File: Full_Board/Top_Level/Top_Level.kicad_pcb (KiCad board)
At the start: 2 copper layers, 218 parts, among them IC1 DRV8824QPWPRQ1, IC2 DRV8824QPWPRQ1, IC3 DRV8824QPWPRQ1, IC4 LM2576HVS-5.0_NOPB, IC5 CD74HC4051PWT, IC6 CD74HC4051PWT, IC7 DRV8210DRLR, J1 OQ0212500000G, J1-J1 Conn_01x10, J10 KLDHCX-8-0202-A, J11 OQ0212500000G, J12 OQ0432500000G, J13 OQ0432500000G, J15 OQ0432500000G, J16 OQ0432500000G, J17 OQ0432500000G, J18 OQ0432500000G, J19 OQ0432500000G, J2 OQ0212500000G, J20 OQ0432500000G, J21 OQ0212500000G, J22 OQ0212500000G, J23 OQ0212500000G, J24 OQ0212500000G, J3 OQ0432500000G, J4 OQ0432500000G, J4-J1 Conn_01x10, J5 OQ0432500000G, J5-J1 Conn_01x10, J6 USB_A, J7 OQ0212500000G, J8 OQ0212500000G, J8-J1 Conn_01x10, J9 OQ0212500000G, U1 UCLAMP3301H.TCT, U10 LM2576SX-3.3-NOPB, U11 UCLAMP3301H.TCT, U12 UCLAMP3301H.TCT, U13 UCLAMP3301H.TCT, U14 UCLAMP3301H.TCT, U15 UCLAMP3301H.TCT, U16 UCLAMP3301H.TCT, U17 UCLAMP3301H.TCT, U18 UCLAMP3301H.TCT, U2 UCLAMP3301H.TCT, U3 UCLAMP3301H.TCT, U4 UCLAMP3301H.TCT, U5 UCLAMP3301H.TCT, U6 UCLAMP3301H.TCT, U7 JS102011SCQN, U8 UCLAMP3301H.TCT, U9 UCLAMP3301H.TCT

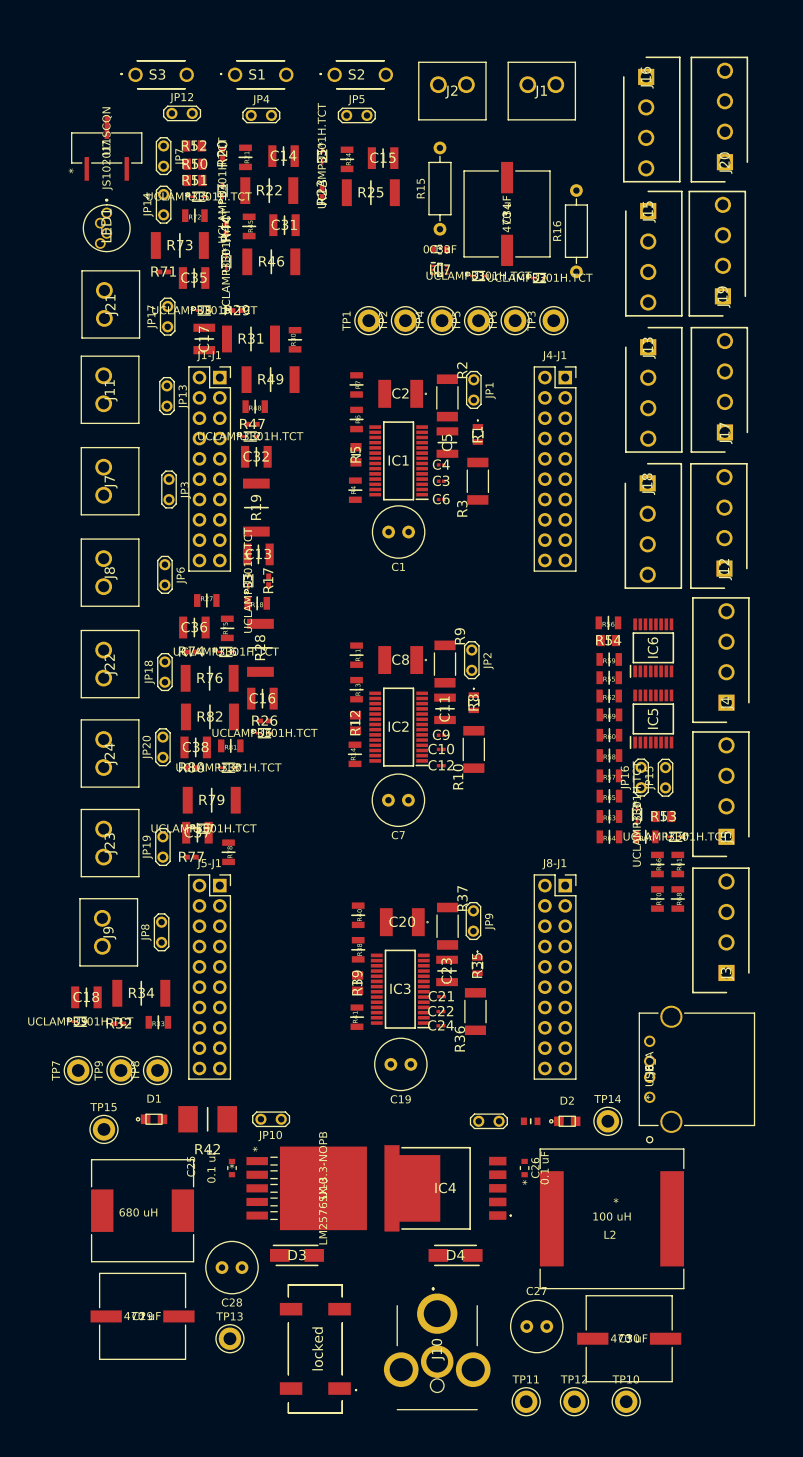
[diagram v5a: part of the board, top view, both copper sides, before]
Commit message: Add GND plane, GND major ICs
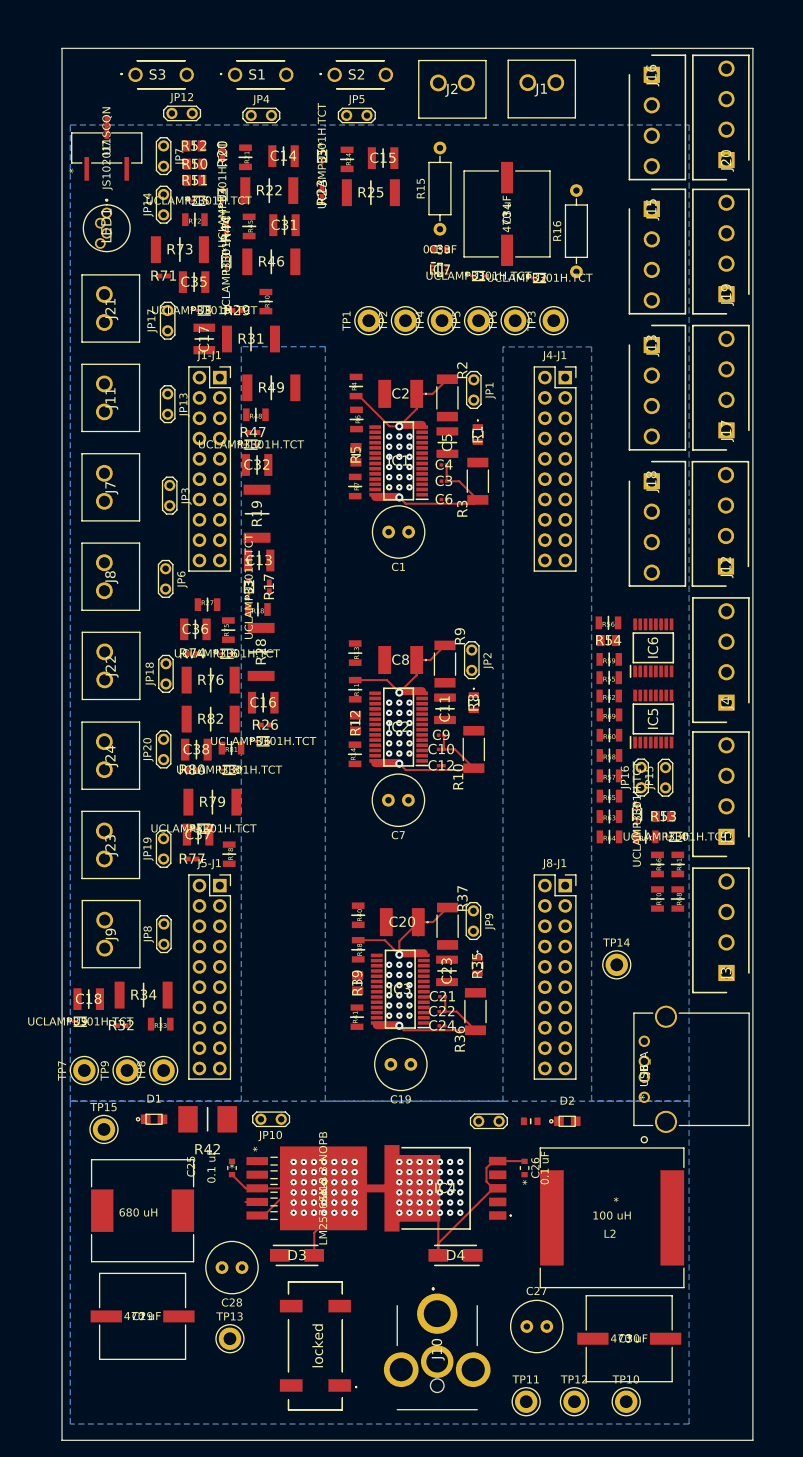
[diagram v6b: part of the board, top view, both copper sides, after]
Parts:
- moved TP14 19.6 mm to (123.8, 133.9)
- moved R4 13.0 mm to (92.0, 60.0)
- moved R7 12.7 mm to (90.3, 75.7)
- moved R30 5.49 mm to (79.1, 52.6), turned to 90 degrees
- moved R13 4.57 mm to (90.3, 96.5)
- moved R11 4.32 mm to (90.3, 101.1)
- moved U6 1.03 mm to (79.6, 105.9)
- moved U12 1.02 mm to (78.1, 68.8)
- moved R47 1.02 mm to (78.3, 67.3)
- moved R48 1.02 mm to (77.1, 64.3)
- moved JP13 1.02 mm to (67.7, 62.5)
- moved J11 1.02 mm to (59.7, 61.2)
- moved R49 1.02 mm to (80.6, 61.7)
- moved C32 1.02 mm to (78.8, 71.4)
- moved R17 0.77 mm to (80.4, 86.6)
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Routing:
- net GND: track 0.00 -> 198.6 mm, vias 0 -> 144
- net Net-(D3-Pad1): track 0.00 -> 2.27 mm
- added copper zone on B.Cu, net GND
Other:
- board outline added: 86.4 x 174 mm

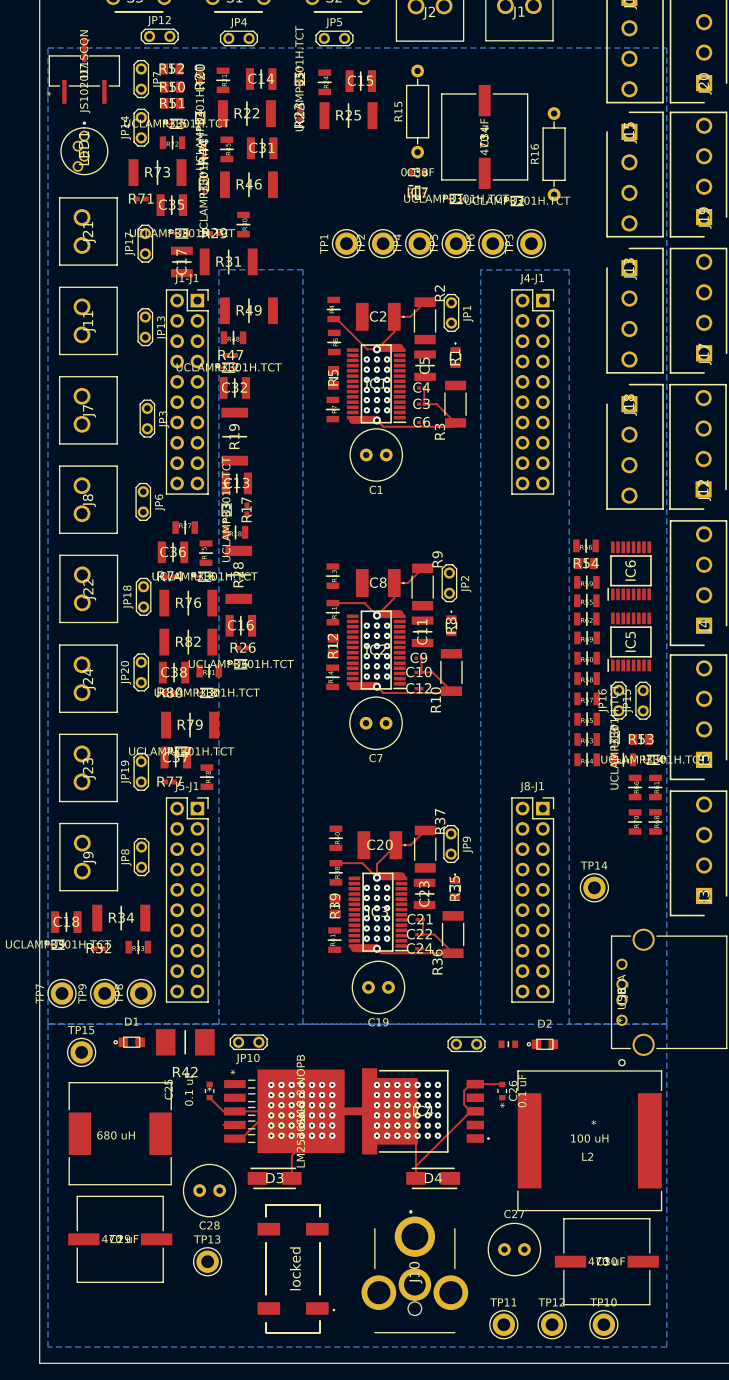
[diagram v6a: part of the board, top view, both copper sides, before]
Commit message: Merge GND planes, update gitignore rules
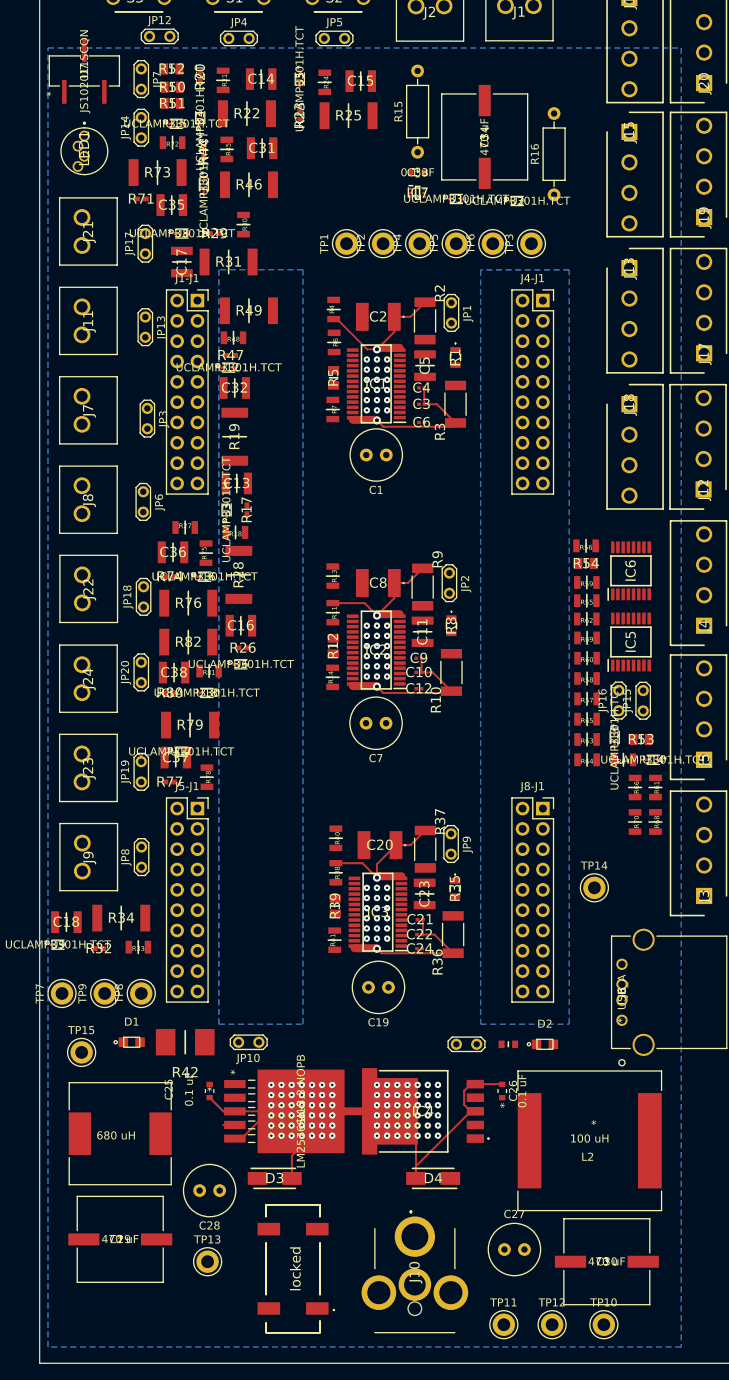
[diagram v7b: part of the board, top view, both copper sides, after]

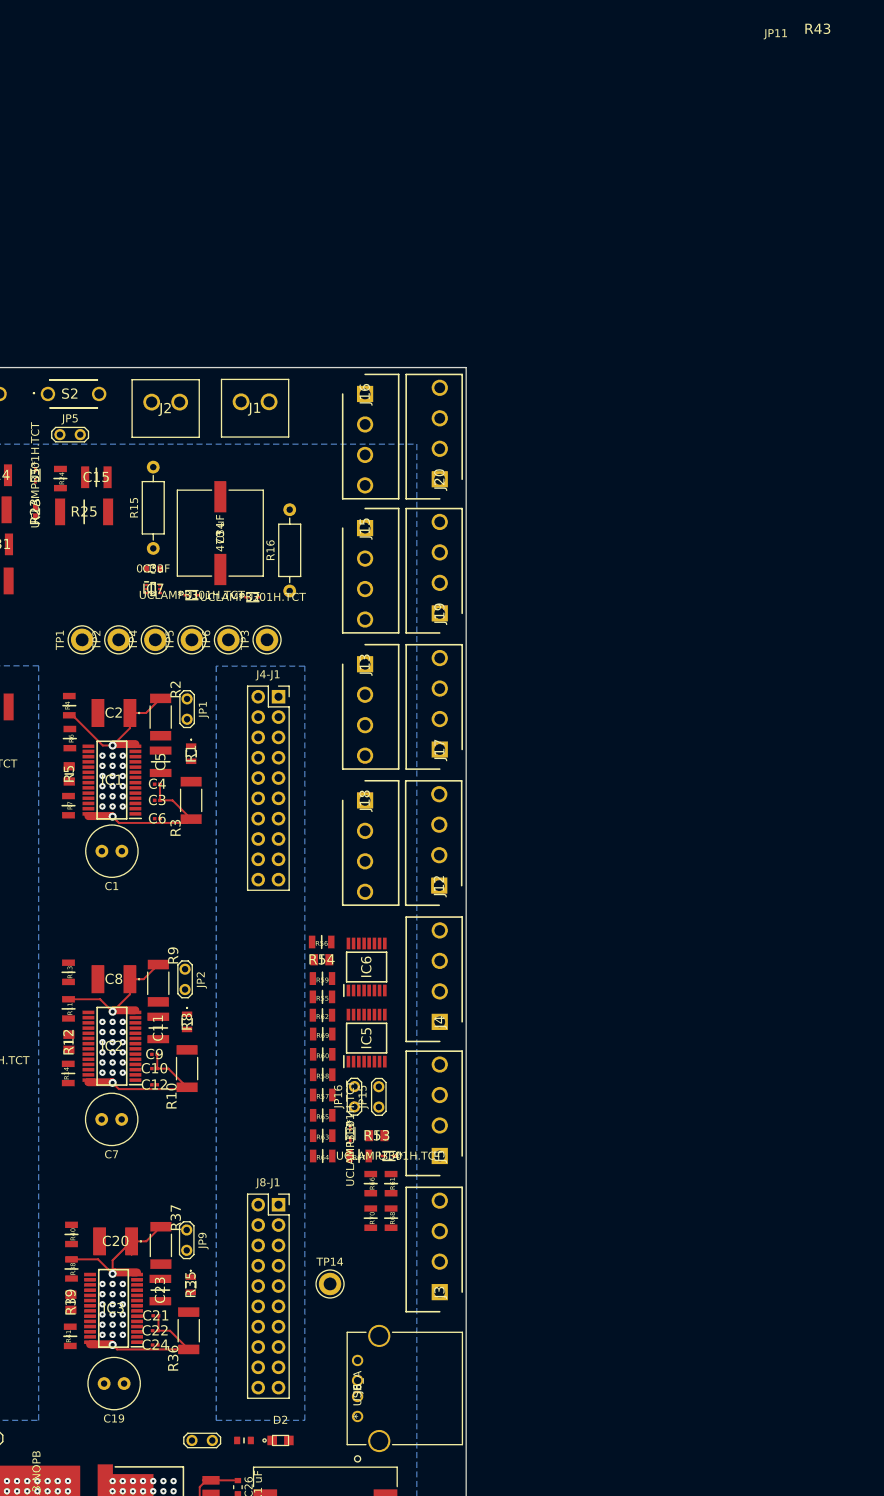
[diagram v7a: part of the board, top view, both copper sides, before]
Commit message: Adjust stepper placement for heatsinks
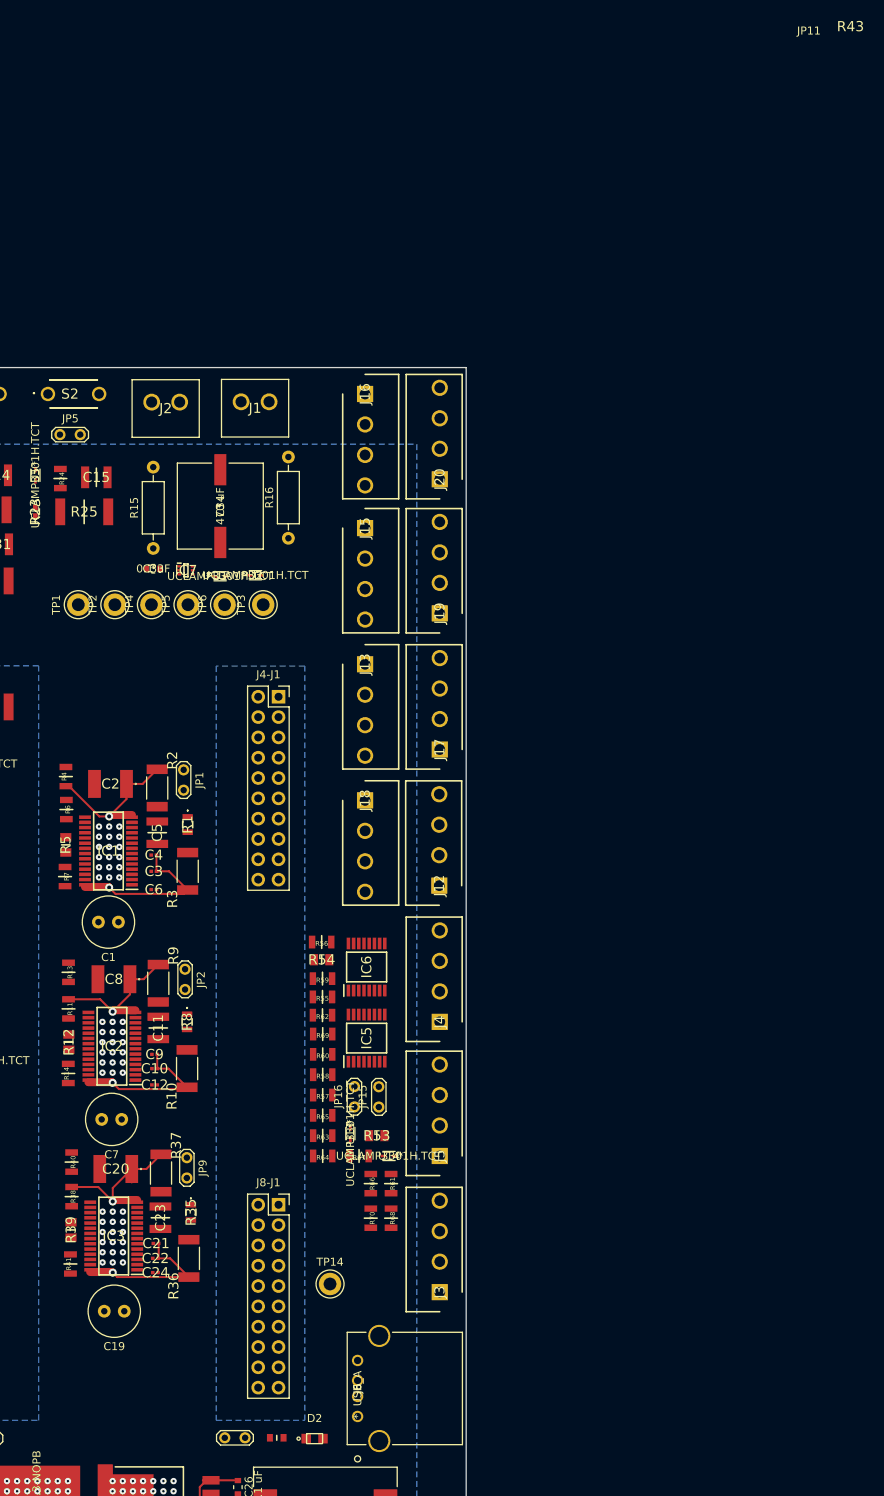
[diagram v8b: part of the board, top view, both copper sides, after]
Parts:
- moved C19 9.04 mm to (98.1, 137.3)
- moved C20 9.04 mm to (97.0, 119.5)
- moved C21 9.04 mm to (102.0, 128.8)
- moved C23 9.04 mm to (102.6, 125.6)
- moved C24 9.04 mm to (102.0, 132.4)
- moved IC3 9.04 mm to (96.7, 127.9)
- moved JP9 9.04 mm to (105.9, 118.1)
- moved R35 9.04 mm to (106.4, 124.9)
- moved R37 9.04 mm to (102.7, 120.0)
- moved R38 9.04 mm to (90.7, 124.5)
- moved R39 9.04 mm to (91.4, 127.1)
- moved R40 9.04 mm to (90.7, 120.2)
- moved R41 9.04 mm to (92.1, 129.8)
- moved C22 9.04 mm to (102.0, 130.7)
- moved R36 9.04 mm to (106.1, 130.7)
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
